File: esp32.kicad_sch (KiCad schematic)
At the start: 25 parts, among them IC4 TPS22917DBVR, IC5 TPS22917DBVR, IC6 TPS22917DBVR, J19 ESP GPIOs, J6 UART, U4 ESP32-WROOM-32U

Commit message: Fixed a lot of things
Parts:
- removed R12: 2k2, Resistor_SMD:R_0603_1608Metric_Pad0.98x0.95mm_HandSolder, symbol Device:R_Small
- added R10: 2k2, Resistor_SMD:R_0603_1608Metric_Pad0.98x0.95mm_HandSolder, symbol Device:R_Small
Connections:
- net PA0: now also R10.2; no longer J6.2 (Pin_2)
- net PA1: now also U4.28 (IO17); no longer J6.1 (Pin_1), U4.35 (TXD0/IO1)
- net at U4.27 (IO16): now also R10.1
- net ESP_UART0_RX: now reaches U4.34 (RXD0/IO3)
- net ESP_UART0_RX: now also J6.2 (Pin_2)
- new net ESP_UART0_TX: J6.1 (Pin_1), U4.35 (TXD0/IO1)
- no-connect marks 27 -> 25
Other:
- note added: "ESP UART2 RX"
- note added: "ESP UART2 TX"
- note added: "STM32 UART4 RX"
- note added: "STM32 UART4 TX"
- moved on the sheet: J6
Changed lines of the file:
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@@
 	(generator_version "9.0")
 	(paper "A4")
+	(text "STM32 UART4 TX"
+		(exclude_from_sim no)
+		(at 269.494 72.898 0)
+		(effects
+			(font
+				(size 0.762 0.762)
+			)
+		)
+	)
+	(text "STM32 UART4 RX"
+		(exclude_from_sim no)
+		(at 268.986 80.264 0)
+		(effects
+			(font
+				(size 0.762 0.762)
+			)
+		)
+	)
+	(text "ESP UART2 RX"
+		(exclude_from_sim no)
+		(at 243.586 74.168 0)
+		(effects
+			(font
+				(size 0.762 0.762)
+			)
+		)
+	)
+	(text "ESP UART2 TX"
+		(exclude_from_sim no)
+		(at 243.586 76.708 0)
+		(effects
+			(font
+				(size 0.762 0.762)
+			)
+		)
+	)
 	(junction
 		(at 52.07 147.32)
@@
 	)
 	(no_connect
-		(at 238.76 77.47)
-	)
-	(no_connect
 		(at 238.76 80.01)
 	)
@@
 	)
 	(no_connect
-		(at 238.76 74.93)
-	)
-	(no_connect
 		(at 86.36 107.95)
 	)
@@
 	(wire
 		(pts
+			(xy 238.76 74.93) (xy 252.73 74.93)
+		)
+		(stroke
+			(width 0)
+			(type default)
+		)
+	)
+	(wire
+		(pts
 			(xy 31.75 72.39) (xy 31.75 74.93)
 		)
@@
 	(wire
 		(pts
-			(xy 257.81 55.88) (xy 254 55.88)
-		)
-		(stroke
-			(width 0)
-			(type default)
-		)
-	)
-	(wire
-		(pts
 			(xy 119.38 139.7) (xy 149.86 139.7)
 		)
@@
 	(wire
 		(pts
+			(xy 238.76 77.47) (xy 266.7 77.47)
+		)
+		(stroke
+			(width 0)
+			(type default)
+		)
+	)
+	(wire
+		(pts
 			(xy 58.42 40.64) (xy 31.75 40.64)
 		)
@@
 	(wire
 		(pts
+			(xy 266.7 74.93) (xy 257.81 74.93)
+		)
+		(stroke
+			(width 0)
+			(type default)
+		)
+	)
+	(wire
+		(pts
 			(xy 96.52 139.7) (xy 106.68 139.7)
 		)
@@
 	(wire
 		(pts
-			(xy 248.92 55.88) (xy 242.57 55.88)
+			(xy 242.57 55.88) (xy 257.81 55.88)
 		)
 		(stroke
@@
 		)
 	)
+	(label "ESP_UART0_RX"
+		(at 257.81 55.88 0)
+		(effects
+			(font
+				(size 1.27 1.27)
+			)
+			(justify left bottom)
+		)
+	)
 	(label "ESP_EN"
 		(at 39.37 139.7 180)
@@
 		)
 	)
+	(label "ESP_UART0_TX"
+		(at 257.81 52.07 0)
+		(effects
+			(font
+				(size 1.27 1.27)
+			)
+			(justify left bottom)
+		)
+	)
 	(label "IO4"
 		(at 198.12 137.16 0)
@@
 		)
 	)
+	(label "ESP_UART0_RX"
+		(at 163.83 143.51 0)
+		(effects
+			(font
+				(size 1.27 1.27)
+			)
+			(justify left bottom)
+		)
+	)
 	(label "ESP_ON"
 		(at 88.9 173.99 0)
@@
 		)
 	)
+	(label "ESP_UART0_TX"
+		(at 163.83 140.97 0)
+		(effects
+			(font
+				(size 1.27 1.27)
+			)
+			(justify left bottom)
+		)
+	)
 	(label "NOTE_ON"
 		(at 58.42 107.95 180)
@@
 	(global_label "PA0"
 		(shape passive)
-		(at 176.53 143.51 0)
-		(fields_autoplaced yes)
-		(effects
-			(font
-				(size 1.27 1.27)
-			)
-			(justify left)
-		)
-		(property "Intersheetrefs" "${INTERSHEET_REFS}"
-			(at 181.972 143.51 0)
-			(effects
-				(font
-					(size 1.27 1.27)
-				)
-				(justify left)
-				(hide yes)
-			)
-		)
-	)
-	(global_label "PA0"
-		(shape passive)
-		(at 257.81 55.88 0)
-		(fields_autoplaced yes)
-		(effects
-			(font
-				(size 1.27 1.27)
-			)
-			(justify left)
-		)
-		(property "Intersheetrefs" "${INTERSHEET_REFS}"
-			(at 263.252 55.88 0)
-			(effects
-				(font
-					(size 1.27 1.27)
-				)
-				(justify left)
-				(hide yes)
-			)
-		)
-	)
-	(global_label "PA1"
-		(shape passive)
-		(at 257.81 52.07 0)
+		(at 266.7 74.93 0)
 		(fields_autoplaced yes)
 		(effects
@@
 		)
 		(property "Intersheetrefs" "${INTERSHEET_REFS}"
-			(at 263.252 52.07 0)
+			(at 272.142 74.93 0)
 			(effects
 				(font
@@
 	(global_label "PA1"
 		(shape passive)
-		(at 176.53 140.97 0)
+		(at 266.7 77.47 0)
 		(fields_autoplaced yes)
 		(effects
@@
 		)
 		(property "Intersheetrefs" "${INTERSHEET_REFS}"
-			(at 181.972 140.97 0)
+			(at 272.142 77.47 0)
 			(effects
 				(font
@@
 	)
 	(symbol
-		(lib_id "Device:C")
-		(at 201.93 39.37 0)
+		(lib_id "Device:R_Small")
+		(at 255.27 74.93 90)
 		(unit 1)
 		(exclude_from_sim no)
@@
 		(dnp no)
 		(fields_autoplaced yes)
-		(property "Reference" "C62"
-			(at 205.74 38.0999 0)
+		(property "Reference" "R10"
+			(at 255.27 69.85 90)
 			(effects
 				(font
 					(size 1.27 1.27)
 				)
-				(justify left)
 			)
 		)
-		(property "Value" "100n"
-			(at 205.74 40.6399 0)
+		(property "Value" "2k2"
+			(at 255.27 72.39 90)
 			(effects
 				(font
 					(size 1.27 1.27)
 				)
-				(justify left)
 			)
 		)
-		(property "Footprint" "Capacitor_SMD:C_0603_1608Metric_Pad1.08x0.95mm_HandSolder"
-			(at 202.8952 43.18 0)
+		(property "Footprint" "Resistor_SMD:R_0603_1608Metric_Pad0.98x0.95mm_HandSolder"
+			(at 255.27 74.93 0)
 			(effects
 				(font
@@
 		)
 		(property "Datasheet" "~"
-			(at 201.93 39.37 0)
+			(at 255.27 74.93 0)
 			(effects
 				(font
@@
 			)
 		)
-		(property "Description" "Unpolarized capacitor"
-			(at 201.93 39.37 0)
+		(property "Description" "Resistor, small symbol"
+			(at 255.27 74.93 0)
 			(effects
 				(font
@@
 			)
 		)
-		(pin "2"
-		)
 		(pin "1"
 		)
+		(pin "2"
+		)
 		(instances
 			(project ""
 				(path "/32c2c747-0685-4927-b759-a1d2bc91875e/a402a0ce-c9ea-466a-871f-9107282f1be8"
-					(reference "C62")
+					(reference "R10")
 					(unit 1)
 				)
@@
 	)
 	(symbol
-		(lib_id "Device:R_Small")
-		(at 251.46 55.88 90)
-		(mirror x)
+		(lib_id "Device:C")
+		(at 201.93 39.37 0)
 		(unit 1)
 		(exclude_from_sim no)
@@
 		(on_board yes)
 		(dnp no)
-		(property "Reference" "R12"
-			(at 251.46 60.96 90)
+		(fields_autoplaced yes)
+		(property "Reference" "C62"
+			(at 205.74 38.0999 0)
 			(effects
 				(font
 					(size 1.27 1.27)
 				)
+				(justify left)
 			)
 		)
-		(property "Value" "2k2"
-			(at 251.46 58.42 90)
+		(property "Value" "100n"
+			(at 205.74 40.6399 0)
 			(effects
 				(font
 					(size 1.27 1.27)
 				)
+				(justify left)
 			)
 		)
-		(property "Footprint" "Resistor_SMD:R_0603_1608Metric_Pad0.98x0.95mm_HandSolder"
-			(at 251.46 55.88 0)
+		(property "Footprint" "Capacitor_SMD:C_0603_1608Metric_Pad1.08x0.95mm_HandSolder"
+			(at 202.8952 43.18 0)
 			(effects
 				(font
@@
 		)
 		(property "Datasheet" "~"
-			(at 251.46 55.88 0)
+			(at 201.93 39.37 0)
 			(effects
 				(font
@@
 			)
 		)
-		(property "Description" "Resistor, small symbol"
-			(at 251.46 55.88 0)
+		(property "Description" "Unpolarized capacitor"
+			(at 201.93 39.37 0)
 			(effects
 				(font
@@
 		)
 		(instances
-			(project "telemetry-rusolar-rework"
+			(project ""
 				(path "/32c2c747-0685-4927-b759-a1d2bc91875e/a402a0ce-c9ea-466a-871f-9107282f1be8"
-					(reference "R12")
+					(reference "C62")
 					(unit 1)
 				)
@@
 	(symbol
 		(lib_id "Connector:Conn_01x02_Pin")
-		(at 171.45 140.97 0)
+		(at 158.75 140.97 0)
 		(unit 1)
 		(exclude_from_sim no)
@@
 		(fields_autoplaced yes)
 		(property "Reference" "J6"
-			(at 172.085 135.89 0)
+			(at 159.385 135.89 0)
 			(effects
 				(font
@@
 		)
 		(property "Value" "UART"
-			(at 172.085 138.43 0)
+			(at 159.385 138.43 0)
 			(effects
 				(font
@@
 		)
 		(property "Footprint" "Connector_PinHeader_2.00mm:PinHeader_1x02_P2.00mm_Vertical"
-			(at 171.45 140.97 0)
+			(at 158.75 140.97 0)
 			(effects
 				(font
@@
 		)
 		(property "Datasheet" "~"
-			(at 171.45 140.97 0)
+			(at 158.75 140.97 0)
 			(effects
 				(font
@@
 		)
 		(property "Description" "Generic connector, single row, 01x02, script generated"
-			(at 171.45 140.97 0)
+			(at 158.75 140.97 0)
 			(effects
 				(font

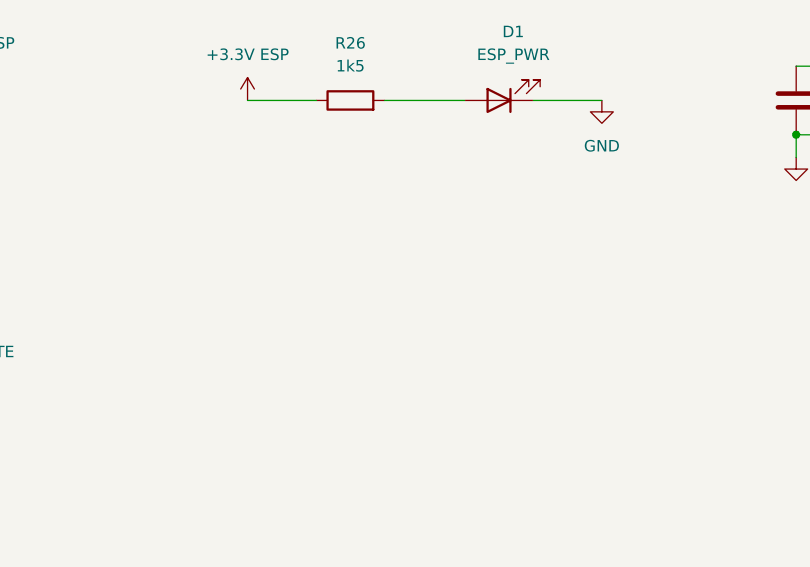
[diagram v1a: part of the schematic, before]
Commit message: Added module LEDs, I2C for Blues Com
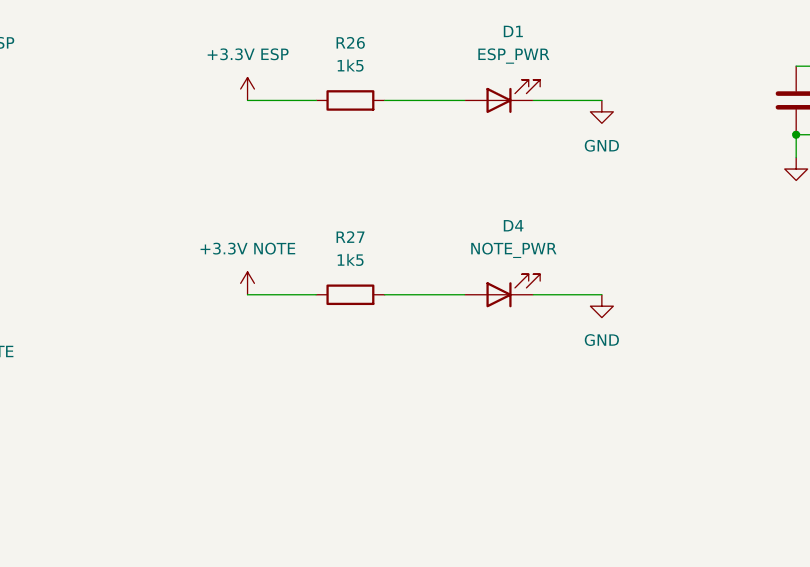
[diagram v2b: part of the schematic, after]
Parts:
- added D4: NOTE_PWR, LED_SMD:LED_0805_2012Metric_Pad1.15x1.40mm_HandSolder, symbol Device:LED
- added R27: 1k5, Resistor_SMD:R_0603_1608Metric_Pad0.98x0.95mm_HandSolder, symbol Device:R
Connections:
- net +3.3V NOTE: now also R27.1
- net GND: now also D4.1 (K)
- new net: D4.2 (A), R27.2
